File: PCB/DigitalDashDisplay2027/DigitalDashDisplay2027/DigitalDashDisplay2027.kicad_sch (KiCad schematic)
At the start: 25 parts, among them IC2 LMR51430YDDCR, U1 Teensy4.0, U5 TCAN1051VDRQ1

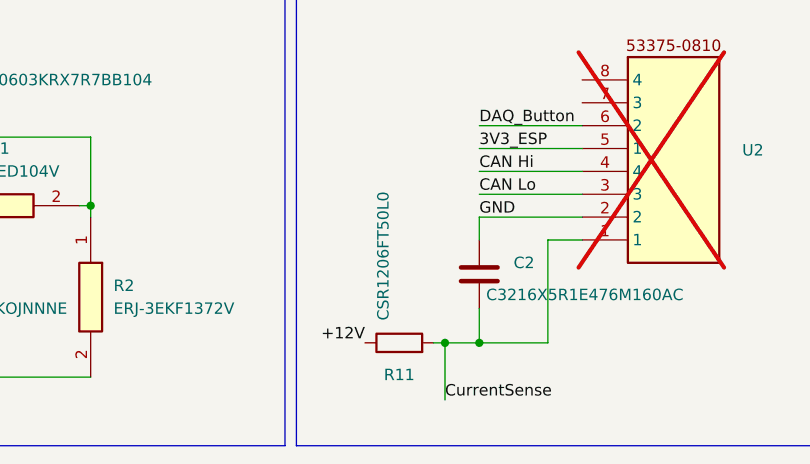
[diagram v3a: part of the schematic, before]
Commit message: Updated BOM and place files for DAQ Board
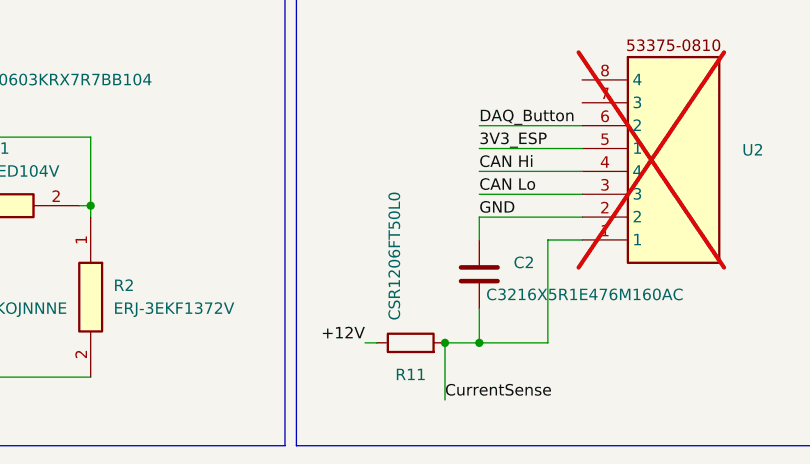
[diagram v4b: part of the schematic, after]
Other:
- moved on the sheet: R11
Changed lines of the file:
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@@
 	)
 	(junction
-		(at 127 185.42)
+		(at 30.48 153.67)
 		(diameter 0)
 		(color 0 0 0 0)
 	)
 	(junction
-		(at 30.48 153.67)
+		(at 127 185.42)
 		(diameter 0)
 		(color 0 0 0 0)
@@
 	(wire
 		(pts
-			(xy 125.73 185.42) (xy 127 185.42)
-		)
-		(stroke
-			(width 0)
-			(type default)
-		)
-	)
-	(wire
-		(pts
 			(xy 35.56 104.14) (xy 35.56 105.41)
 		)
@@
 	(wire
 		(pts
+			(xy 119.38 185.42) (xy 118.11 185.42)
+		)
+		(stroke
+			(width 0)
+			(type default)
+		)
+	)
+	(wire
+		(pts
 			(xy 130.81 185.42) (xy 138.43 185.42)
 		)
@@
 	(symbol
 		(lib_id "Device:R")
-		(at 121.92 185.42 90)
+		(at 123.19 185.42 90)
 		(unit 1)
 		(body_style 1)
@@
 		(dnp no)
 		(property "Reference" "R11"
-			(at 121.92 188.976 90)
+			(at 123.19 188.976 90)
 			(show_name no)
 			(do_not_autoplace no)
@@
 		)
 		(property "Value" "CSR1206FT50L0"
-			(at 120.142 175.768 0)
+			(at 121.412 175.768 0)
 			(show_name no)
 			(do_not_autoplace no)
@@
 		)
 		(property "Footprint" "Resistor_SMD:R_1206_3216Metric"
-			(at 121.92 187.198 90)
+			(at 123.19 187.198 90)
 			(hide yes)
 			(show_name no)
@@
 		)
 		(property "Datasheet" ""
-			(at 121.92 185.42 0)
+			(at 123.19 185.42 0)
 			(hide yes)
 			(show_name no)
@@
 		)
 		(property "Description" "Resistor"
-			(at 121.92 185.42 0)
+			(at 123.19 185.42 0)
 			(hide yes)
 			(show_name no)

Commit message: Updated FFT script to shift data and normalize, updated Dashboard BOM and place files
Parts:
- C2: value C3216X5R1E476M160AC -> C3216X5R1E476MTJ00E
- U4: now not fitted
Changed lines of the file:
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@@
 			)
 		)
-		(property "Value" "C3216X5R1E476M160AC"
+		(property "Value" "C3216X5R1E476MTJ00E"
 			(at 131.572 180.086 0)
 			(show_name no)
@@
 		(on_board yes)
 		(in_pos_files yes)
-		(dnp no)
+		(dnp yes)
 		(fields_autoplaced yes)
 		(property "Reference" "U4"

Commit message: Finalized A-A filters, finishing touches on DAQ and Dash boards
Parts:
- R11, R3, R4: now not fitted
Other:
- note added: "Chip Detect"

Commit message: Finishing touches on dashboard, finished PDM with stitched vias, continued work on dashboard teensy code
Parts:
- added R12: 10k, Resistor_SMD:R_0603_1608Metric_Pad0.98x0.95mm_HandSolder, symbol 1206W4J0103T5E:1206W4J0103T5E
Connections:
- net DAQ_Button: now also R12.1
- net GND: now also R12.2
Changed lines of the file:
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@@
 	)
 	(junction
+		(at 186.69 64.77)
+		(diameter 0)
+		(color 0 0 0 0)
+	)
+	(junction
+		(at 186.69 41.91)
+		(diameter 0)
+		(color 0 0 0 0)
+	)
+	(junction
 		(at 30.48 153.67)
 		(diameter 0)
@@
 	(wire
 		(pts
-			(xy 194.31 41.91) (xy 179.07 41.91)
+			(xy 194.31 41.91) (xy 186.69 41.91)
+		)
+		(stroke
+			(width 0)
+			(type default)
+		)
+	)
+	(wire
+		(pts
+			(xy 179.07 41.91) (xy 186.69 41.91)
 		)
 		(stroke
@@
 	(wire
 		(pts
+			(xy 186.69 64.77) (xy 194.31 64.77)
+		)
+		(stroke
+			(width 0)
+			(type default)
+		)
+	)
+	(wire
+		(pts
 			(xy 195.58 115.57) (xy 213.36 115.57)
 		)
@@
 	(wire
 		(pts
-			(xy 184.15 64.77) (xy 194.31 64.77)
+			(xy 186.69 59.69) (xy 186.69 64.77)
+		)
+		(stroke
+			(width 0)
+			(type default)
+		)
+	)
+	(wire
+		(pts
+			(xy 180.34 64.77) (xy 186.69 64.77)
 		)
 		(stroke
@@
 	)
 	(label "GND"
-		(at 184.15 64.77 0)
+		(at 180.34 64.77 0)
 		(effects
 			(font
@@
 					(unit 1)
 				)
+			)
+		)
+	)
+	(symbol
+		(lib_id "1206W4J0103T5E:1206W4J0103T5E")
+		(at 186.69 41.91 270)
+		(unit 1)
+		(body_style 1)
+		(exclude_from_sim no)
+		(in_bom yes)
+		(on_board yes)
+		(in_pos_files yes)
+		(dnp no)
+		(property "Reference" "R12"
+			(at 189.738 55.118 0)
+			(show_name no)
+			(do_not_autoplace no)
+			(effects
+				(font
+					(size 1.27 1.27)
+				)
+				(justify right)
+			)
+		)
+		(property "Value" "10k"
+			(at 191.77 55.118 0)
+			(show_name no)
+			(do_not_autoplace no)
+			(effects
+				(font
+					(size 1.27 1.27)
+				)
+				(justify right)
+			)
+		)
+		(property "Footprint" "Resistor_SMD:R_0603_1608Metric_Pad0.98x0.95mm_HandSolder"
+			(at 90.5 55.88 0)
+			(hide yes)
+			(show_name no)
+			(do_not_autoplace no)
+			(effects
+				(font
+					(size 1.27 1.27)
+				)
+				(justify left top)
+			)
+		)
+		(property "Datasheet" ""
+			(at -9.5 55.88 0)
+			(hide yes)
+			(show_name no)
+			(do_not_autoplace no)
+			(effects
+				(font
+					(size 1.27 1.27)
+				)
+				(justify left top)
+			)
+		)
+		(property "Description" "10 kOhms ±5% 0.1W, 1/10W"
+			(at 186.69 41.91 0)
+			(hide yes)
+			(show_name no)
+			(do_not_autoplace no)
+			(effects
+				(font
+					(size 1.27 1.27)
+				)
+			)
+		)
+		(property "Height" ""
+			(at -209.5 55.88 0)
+			(hide yes)
+			(show_name no)
+			(do_not_autoplace no)
+			(effects
+				(font
+					(size 1.27 1.27)
+				)
+				(justify left top)
+			)
+		)
+		(property "Manufacturer_Name" "Yageo"
+			(at -309.5 55.88 0)
+			(hide yes)
+			(show_name no)
+			(do_not_autoplace no)
+			(effects
+				(font
+					(size 1.27 1.27)
+				)
+				(justify left top)
+			)
+		)
+		(property "Manufacturer_Part_Number" "RC0603JR-0710KL"
+			(at -409.5 55.88 0)
+			(hide yes)
+			(show_name no)
+			(do_not_autoplace no)
+			(effects
+				(font
+					(size 1.27 1.27)
+				)
+				(justify left top)
+			)
+		)
+		(property "Mouser Part Number" ""
+			(at -509.5 55.88 0)
+			(hide yes)
+			(show_name no)
+			(do_not_autoplace no)
+			(effects
+				(font
+					(size 1.27 1.27)
+				)
+				(justify left top)
+			)
+		)
+		(property "Mouser Price/Stock" ""
+			(at -609.5 55.88 0)
+			(hide yes)
+			(show_name no)
+			(do_not_autoplace no)
+			(effects
+				(font
+					(size 1.27 1.27)
+				)
+				(justify left top)
+			)
+		)
+		(property "Arrow Part Number" ""
+			(at -709.5 55.88 0)
+			(hide yes)
+			(show_name no)
+			(do_not_autoplace no)
+			(effects
+				(font
+					(size 1.27 1.27)
+				)
+				(justify left top)
+			)
+		)
+		(property "Arrow Price/Stock" ""
+			(at -809.5 55.88 0)
+			(hide yes)
+			(show_name no)
+			(do_not_autoplace no)
+			(effects
+				(font
+					(size 1.27 1.27)
+				)
+				(justify left top)
+			)
+		)
+		(pin "1"
+		)
+		(pin "2"
+		)
+		(instances
+			(project "DigitalDashDisplay2027"
+				(path "/fd3c9ef8-c48c-474c-8aa9-920e9693aa71"
+					(reference "R12")
+					(unit 1)
+				)
